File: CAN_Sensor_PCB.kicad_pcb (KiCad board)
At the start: 2 copper layers, 59 x 32.5 mm, 63 parts, among them J1 Conn_01x02, J3 Conn_01x02, J4 Conn_01x04, J5 Conn_01x04, U1 APM32F405RGT6, U2 LM2594HVM-3.3

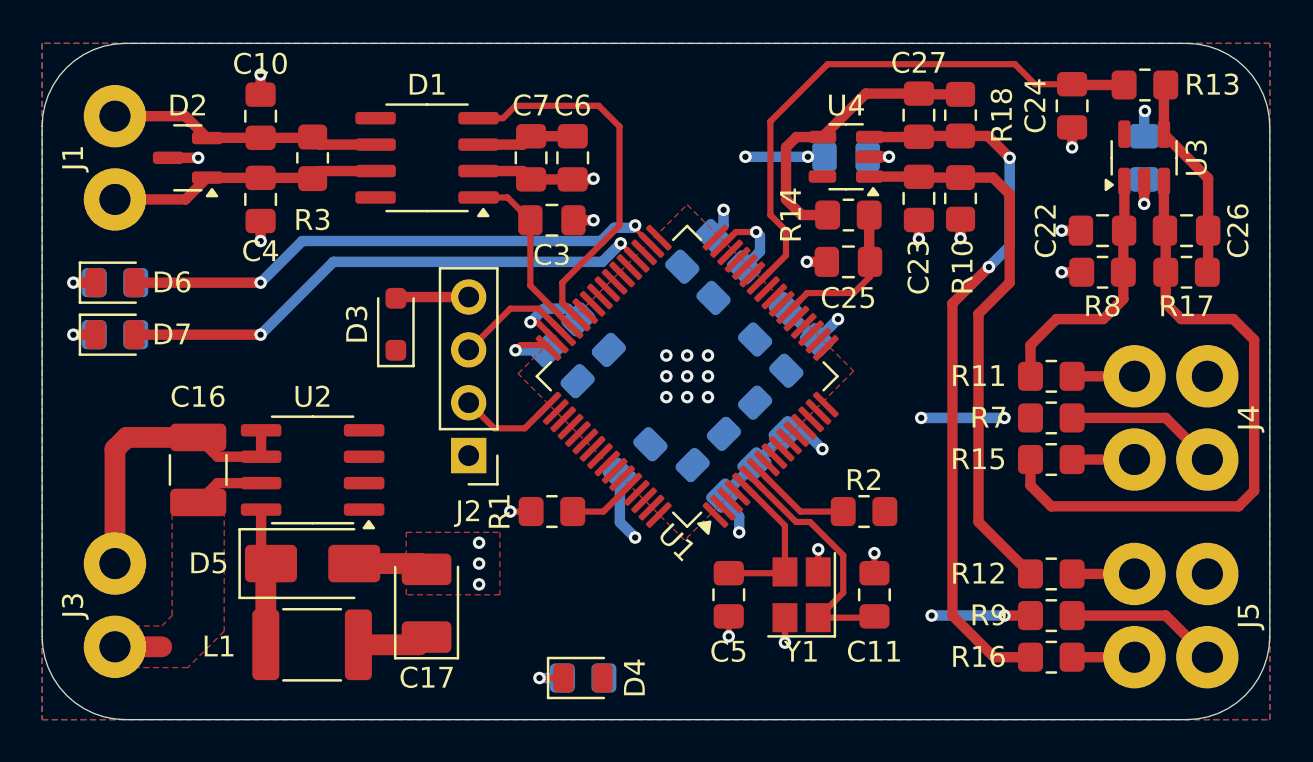
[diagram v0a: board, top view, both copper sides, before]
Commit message: VER1.0: заменил два усилителя на один
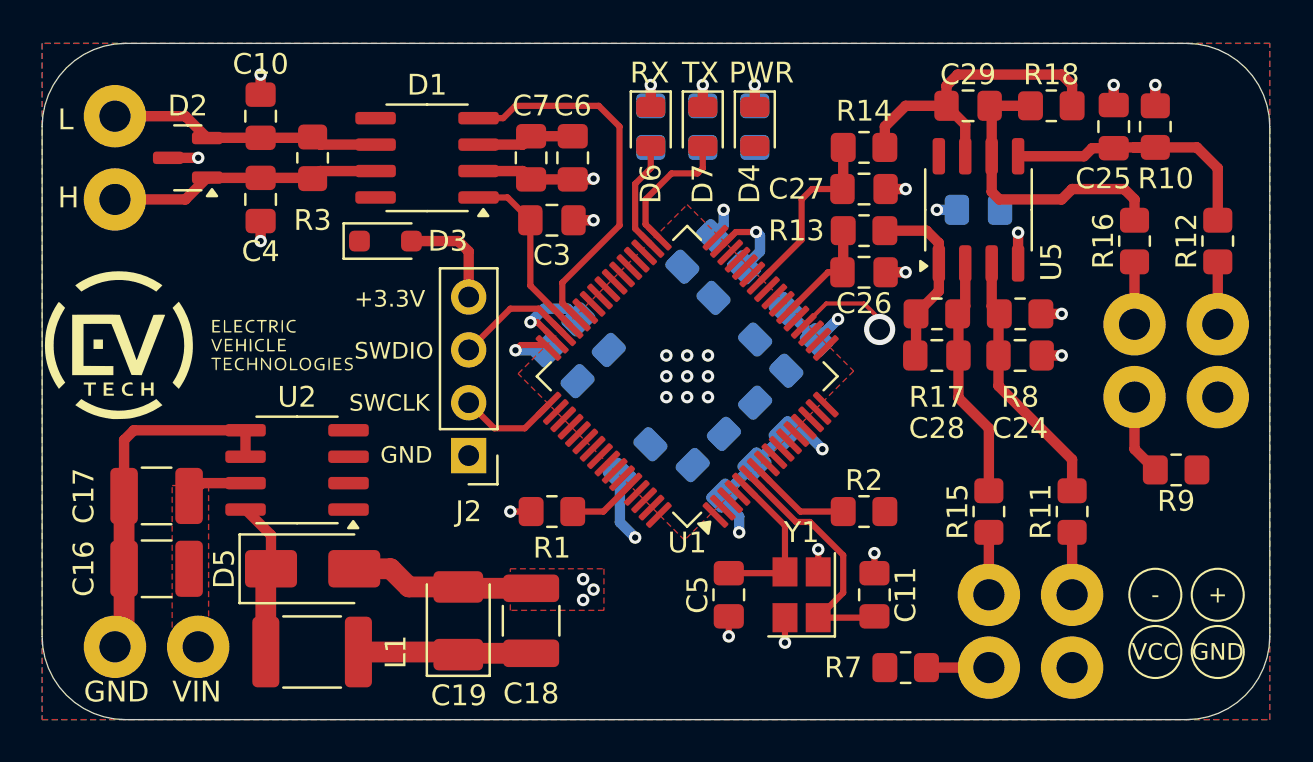
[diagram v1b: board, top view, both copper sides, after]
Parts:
- removed the C21 at (173.1, 129.9)
- removed U3, U4: ~, Package_TO_SOT_SMD:SOT-23-5
- added C16: 10u, Capacitor_SMD:C_1210_3225Metric_Pad1.33x2.70mm_HandSolder, F.Cu at (140.0, 149.8)
- added C18: 10u, Capacitor_SMD:C_1210_3225Metric_Pad1.33x2.70mm_HandSolder, F.Cu at (158.0, 152.2)
- added G***: LOGO, Logo_My:EV_Tech_15mm, F.Cu at (142.0, 139.0)
- added U5: LMV358, Package_SO:SO-8_3.9x4.9mm_P1.27mm, F.Cu at (179.5, 132.5)
- moved D7 30.0 mm to (166.2, 128.5), turned to -90 degrees
- moved R6 30.0 mm to (166.2, 128.5), turned to -90 degrees
- moved D4 27.8 mm to (168.8, 128.5), turned to -90 degrees
- moved R4 27.8 mm to (168.8, 128.5), turned to -90 degrees
- moved D6 26.8 mm to (163.8, 128.5), turned to -90 degrees
- moved R5 26.8 mm to (163.8, 128.5), turned to -90 degrees
- moved R16 20.4 mm to (187.0, 134.0), turned to -90 degrees
- moved R12 17.9 mm to (191.0, 134.0), turned to -90 degrees
- moved R13 15.2 mm to (174.0, 133.5)
- moved R7 13.9 mm to (176.0, 154.5)
- moved C28 13.4 mm to (177.5, 139.5), turned to 180 degrees
- moved C26 12.8 mm to (174.0, 135.5), turned to 0 degrees
- moved J4 12.6 mm to (182.0, 153.0), turned to 180 degrees
- moved R17 12.2 mm to (177.5, 137.5), turned to 0 degrees
- moved J5 12.0 mm to (189.0, 140.0), turned to 180 degrees
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- renumbered C16 to C17, C17 to C19, C18 to C20, C19 to C21, C20 to C22, C22 to C24, C23 to C25, C24 to C26, C25 to C27, C26 to C28, C27 to C29
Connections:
- C26 pad 1: PTC1_SENSE -> PTC2_SENSE
- C27 pad 1: PTC2_SENSE -> PTC1_SENSE
- R13 pad 1: PTC1_SENSE -> PTC2_SENSE
- R14 pad 1: PTC2_SENSE -> PTC1_SENSE
- U1 pad 33: unconnected-(U1-PB12-Pad33) -> Net-(D7-A)
- U1 pad 36: Net-(D7-A) -> unconnected-(U1-PB15-Pad36)
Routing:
- net Net-(D6-A): track 26.5 -> 5.39 mm, vias 2 -> 0
- net Net-(U5B--): track 34.9 -> 14.6 mm, vias 2 -> 0
- net Net-(D7-A): track 26.3 -> 6.53 mm, vias 2 -> 0
- net Net-(U5A--): track 30.8 -> 11.7 mm
- net PTC1_SENSE: track 27.1 -> 8.98 mm
- net Net-(U5B-+): track 27.0 -> 13.6 mm
- net GND: track 40.9 -> 49.0 mm, vias 30 -> 29
- net +3.3V: track 41.9 -> 34.1 mm, vias 13 -> 7
- net DAC_OUT1: track 0.00 -> 4.90 mm, vias 0 -> 1
- net Net-(J4-Pin_4): track 7.33 -> 3.00 mm
- net Net-(J5-Pin_4): track 7.33 -> 3.91 mm
- net +24V: track 5.66 -> 2.97 mm
- net PTC2_SENSE: track 7.56 -> 5.36 mm
- net Net-(D3-A): track 3.52 -> 5.15 mm
- net Net-(C29-Pad2): track 14.3 -> 15.6 mm
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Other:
- board text added: "+"
- board text added: "+3.3V"
- board text added: "-"
- board text added: "GND"
- board text added: "H"
- board text added: "L"
- board text added: "PWR"
- board text added: "RX"
- board text added: "SWCLK"
- board text added: "SWDIO"
- board text added: "TX"
- board text added: "VCC"
- board text added: "VIN"

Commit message: VER1.0: отправил в резонит
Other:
- board text added: "CAN Sensor VER1.0"
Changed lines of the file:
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@@
+		)
+	)
+	(gr_text "CAN Sensor VER1.0"
+		(at 160 156.25 0)
+		(layer "F.SilkS")
+		(effects
+			(font
+				(size 0.8 0.8)
+				(thickness 0.16)
+				(bold yes)
+				(italic yes)
+			)
+			(justify left bottom)
 		)
 	)

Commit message: VER1.0: добавил схему по госту в доки
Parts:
- D5: value MBRA320 -> ~
- J1, J3: value Conn_01x02 -> ~
- J4, J5: value Conn_01x04 -> ~
- U1: value APM32F405RGT6 -> ~
- U2: value LM2594HVM-3.3 -> ~
- U5: value LMV358 -> ~
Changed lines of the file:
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@@
 			)
 		)
-		(property "Value" "LMV358"
+		(property "Value" "~"
 			(at 0 3.4 90)
 			(layer "F.Fab")
@@
 			)
 		)
+		(property "Product Name" "LM158DR"
+			(at 0 0 90)
+			(unlocked yes)
+			(layer "F.Fab")
+			(hide yes)
+			(effects
+				(font
+					(size 1 1)
+					(thickness 0.15)
+				)
+			)
+		)
 		(property ki_fp_filters "SOIC*3.9x4.9mm*P1.27mm* DIP*W7.62mm* TO*99* OnSemi*Micro8* TSSOP*3x3mm*P0.65mm* TSSOP*4.4x3mm*P0.65mm* MSOP*3x3mm*P0.65mm* SSOP*3.9x4.9mm*P0.635mm* LFCSP*2x2mm*P0.5mm* *SIP* SOIC*5.3x6.2mm*P1.27mm*")
 		(sheetname "/")
@@
 			)
 		)
-		(property "Value" "APM32F405RGT6"
+		(property "Value" "~"
 			(at 0 7.4 135)
 			(layer "F.Fab")
@@
 			)
 		)
+		(property "Product Name" "APM32F405RGT6"
+			(at 0 0 135)
+			(unlocked yes)
+			(layer "F.Fab")
+			(hide yes)
+			(effects
+				(font
+					(size 1 1)
+					(thickness 0.15)
+				)
+			)
+		)
 		(property ki_fp_filters "LQFP*10x10mm*P0.5mm*")
 		(sheetname "/")
@@
 			)
 		)
-		(property "Value" "Conn_01x04"
+		(property "Value" "~"
 			(at 0 -4 180)
 			(unlocked yes)
@@
 			)
 		)
+		(property "Purpose" "PT2"
+			(at 0 0 180)
+			(unlocked yes)
+			(layer "F.Fab")
+			(hide yes)
+			(effects
+				(font
+					(size 1 1)
+					(thickness 0.15)
+				)
+			)
+		)
 		(property ki_fp_filters "Connector*:*_1x??_*")
 		(sheetname "/")
 		(sheetfile "CAN_Sensor_PCB.kicad_sch")
-		(attr through_hole)
+		(attr through_hole dnp)
 		(fp_text user "${REFERENCE}"
 			(at 0 5 180)
@@
 			)
 		)
-		(property "Description P/N" "Blue LED"
+		(property "Description P/N" "LED"
 			(at 0 0 270)
 			(unlocked yes)
@@
 			)
 		)
-		(property "Product Name" "FYLS-0805UBC"
+		(property "Product Name" "FYLS-0805PGC"
 			(at 0 0 270)
 			(unlocked yes)
@@
 			)
 		)
-		(property "Value" "MBRA320"
+		(property "Value" "~"
 			(at 0 2.6 0)
 			(layer "F.Fab")
@@
 			)
 		)
+		(property "Product Name" "MBRA320"
+			(at 0 0 0)
+			(unlocked yes)
+			(layer "F.Fab")
+			(hide yes)
+			(effects
+				(font
+					(size 1 1)
+					(thickness 0.15)
+				)
+			)
+		)
+		(property "Description P/N" "Diode"
+			(at 0 0 0)
+			(unlocked yes)
+			(layer "F.Fab")
+			(hide yes)
+			(effects
+				(font
+					(size 1 1)
+					(thickness 0.15)
+				)
+			)
+		)
 		(property ki_fp_filters "TO-???* *_Diode_* *SingleDiode* D_*")
 		(sheetname "/")
@@
 			)
 		)
+		(property "Product Name" "NLC453232T-470K-PF"
+			(at 0 0 0)
+			(unlocked yes)
+			(layer "F.Fab")
+			(hide yes)
+			(effects
+				(font
+					(size 1 1)
+					(thickness 0.15)
+				)
+			)
+		)
 		(property ki_fp_filters "Choke_* *Coil* Inductor_* L_*")
 		(sheetname "/")
@@
 			)
 		)
-		(property "Description P/N" "Yellow LED"
+		(property "Description P/N" "LED"
 			(at 0 0 270)
 			(unlocked yes)
@@
 			)
 		)
-		(property "Value" "Conn_01x02"
+		(property "Value" "~"
 			(at 0 -3 270)
 			(unlocked yes)
@@
 			)
 		)
+		(property "Purpose" "CAN"
+			(at 0 0 270)
+			(unlocked yes)
+			(layer "F.Fab")
+			(hide yes)
+			(effects
+				(font
+					(size 1 1)
+					(thickness 0.15)
+				)
+			)
+		)
 		(property ki_fp_filters "Connector*:*_1x??_*")
 		(sheetname "/")
 		(sheetfile "CAN_Sensor_PCB.kicad_sch")
-		(attr through_hole)
+		(attr through_hole dnp)
 		(fp_text user "${REFERENCE}"
 			(at 0 3 270)
@@
 			)
 		)
-		(property "Value" "Conn_01x02"
+		(property "Value" "~"
 			(at 0 -3 0)
 			(unlocked yes)
@@
 			)
 		)
+		(property "Purpose" "PWR"
+			(at 0 0 0)
+			(unlocked yes)
+			(layer "F.Fab")
+			(hide yes)
+			(effects
+				(font
+					(size 1 1)
+					(thickness 0.15)
+				)
+			)
+		)
 		(property ki_fp_filters "Connector*:*_1x??_*")
 		(sheetname "/")
 		(sheetfile "CAN_Sensor_PCB.kicad_sch")
 		(zone_connect 1)
-		(attr through_hole)
+		(attr through_hole dnp)
 		(fp_text user "${REFERENCE}"
 			(at 0 3 0)
@@
 			)
 		)
-		(property "Value" "LM2594HVM-3.3"
+		(property "Value" "~"
 			(at 0 3.4 0)
 			(layer "F.Fab")
@@
 			)
 		)
+		(property "Product Name" "LM2594HVM-3.3"
+			(at 0 0 180)
+			(unlocked yes)
+			(layer "F.Fab")
+			(hide yes)
+			(effects
+				(font
+					(size 1 1)
+					(thickness 0.15)
+				)
+			)
+		)
 		(property ki_fp_filters "SOIC*3.9x4.9mm*")
 		(sheetname "/")
@@
 			)
 		)
-		(property "Description P/N" "Blue LED"
+		(property "Description P/N" "LED"
 			(at 0 0 270)
 			(unlocked yes)
@@
 			)
 		)
-		(property "Value" "Conn_01x04"
+		(property "Value" "~"
 			(at 0 -4 180)
 			(unlocked yes)
@@
 			)
 		)
+		(property "Purpose" "PT1"
+			(at 0 0 180)
+			(unlocked yes)
+			(layer "F.Fab")
+			(hide yes)
+			(effects
+				(font
+					(size 1 1)
+					(thickness 0.15)
+				)
+			)
+		)
 		(property ki_fp_filters "Connector*:*_1x??_*")
 		(sheetname "/")
 		(sheetfile "CAN_Sensor_PCB.kicad_sch")
-		(attr through_hole)
+		(attr through_hole dnp)
 		(fp_text user "${REFERENCE}"
 			(at 0 5 180)
@@
 					(thickness 0.15)
 				)
+			)
+		)
+		(property "Product Name" "293D107X96R3B2TE3"
+			(at 0 0 90)
+			(unlocked yes)
+			(layer "F.Fab")
+			(hide yes)
+			(effects
+				(font
+					(size 1 1)
+					(thickness 0.15)
+				)
